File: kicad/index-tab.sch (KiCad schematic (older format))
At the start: 40 parts, among them J1 USB_C_Receptacle_USB2.0, SW1 SW_Push, U1 ATmega32U4-AU, Y1 16MHz

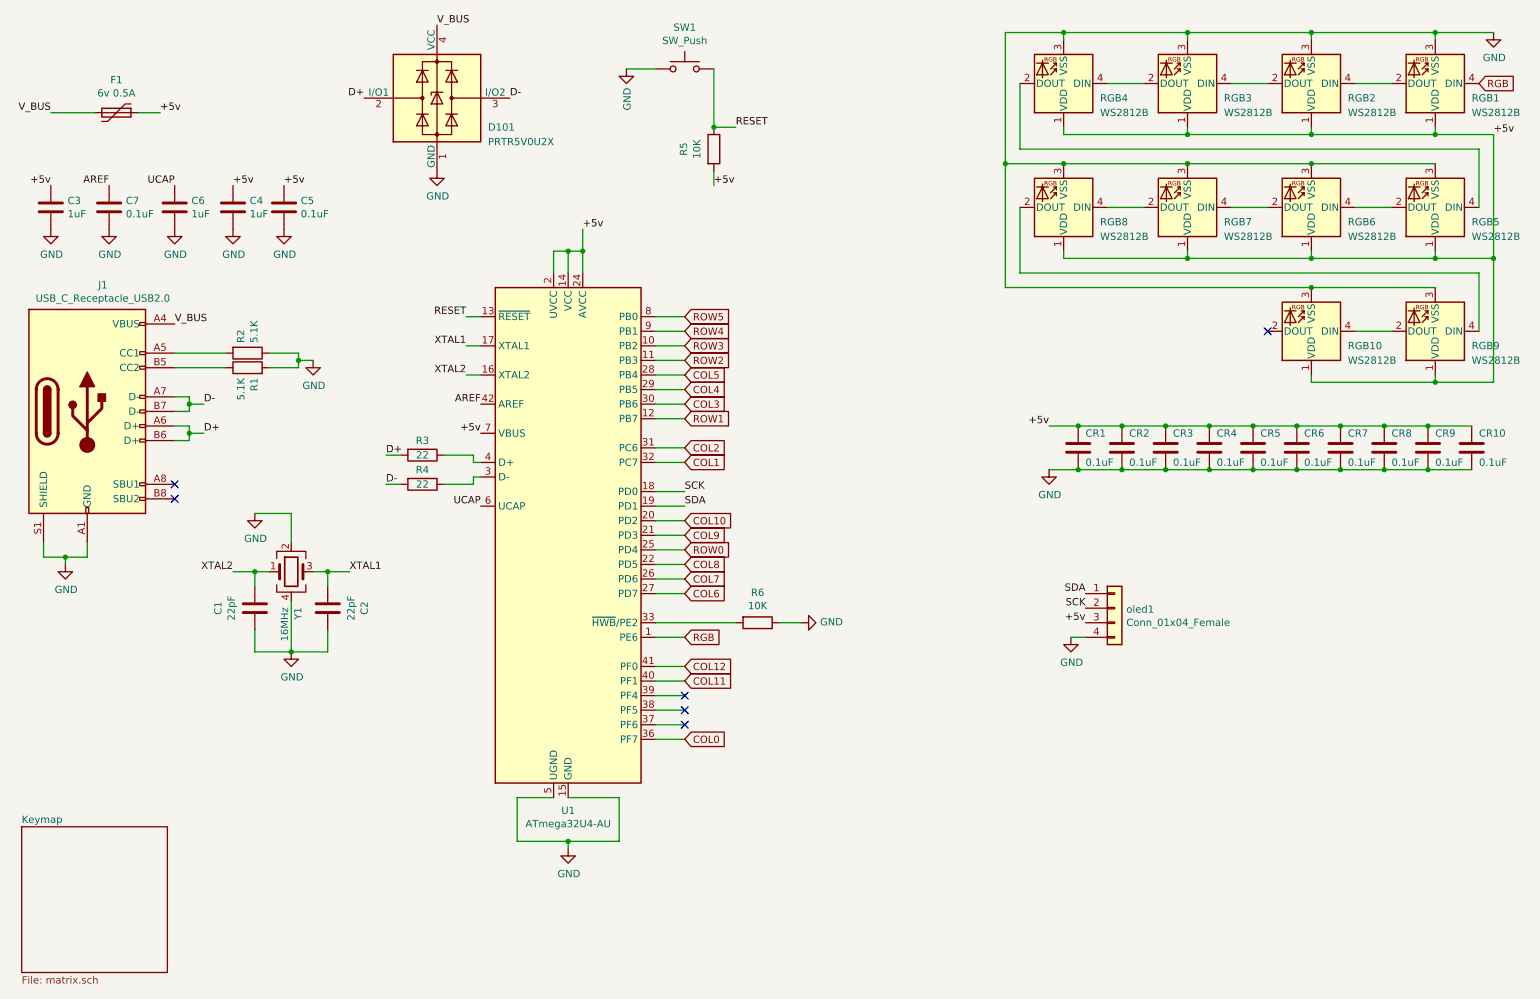
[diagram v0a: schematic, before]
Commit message: rev5: updated schematic
This is heavily inspired by Plain60 by evyd13
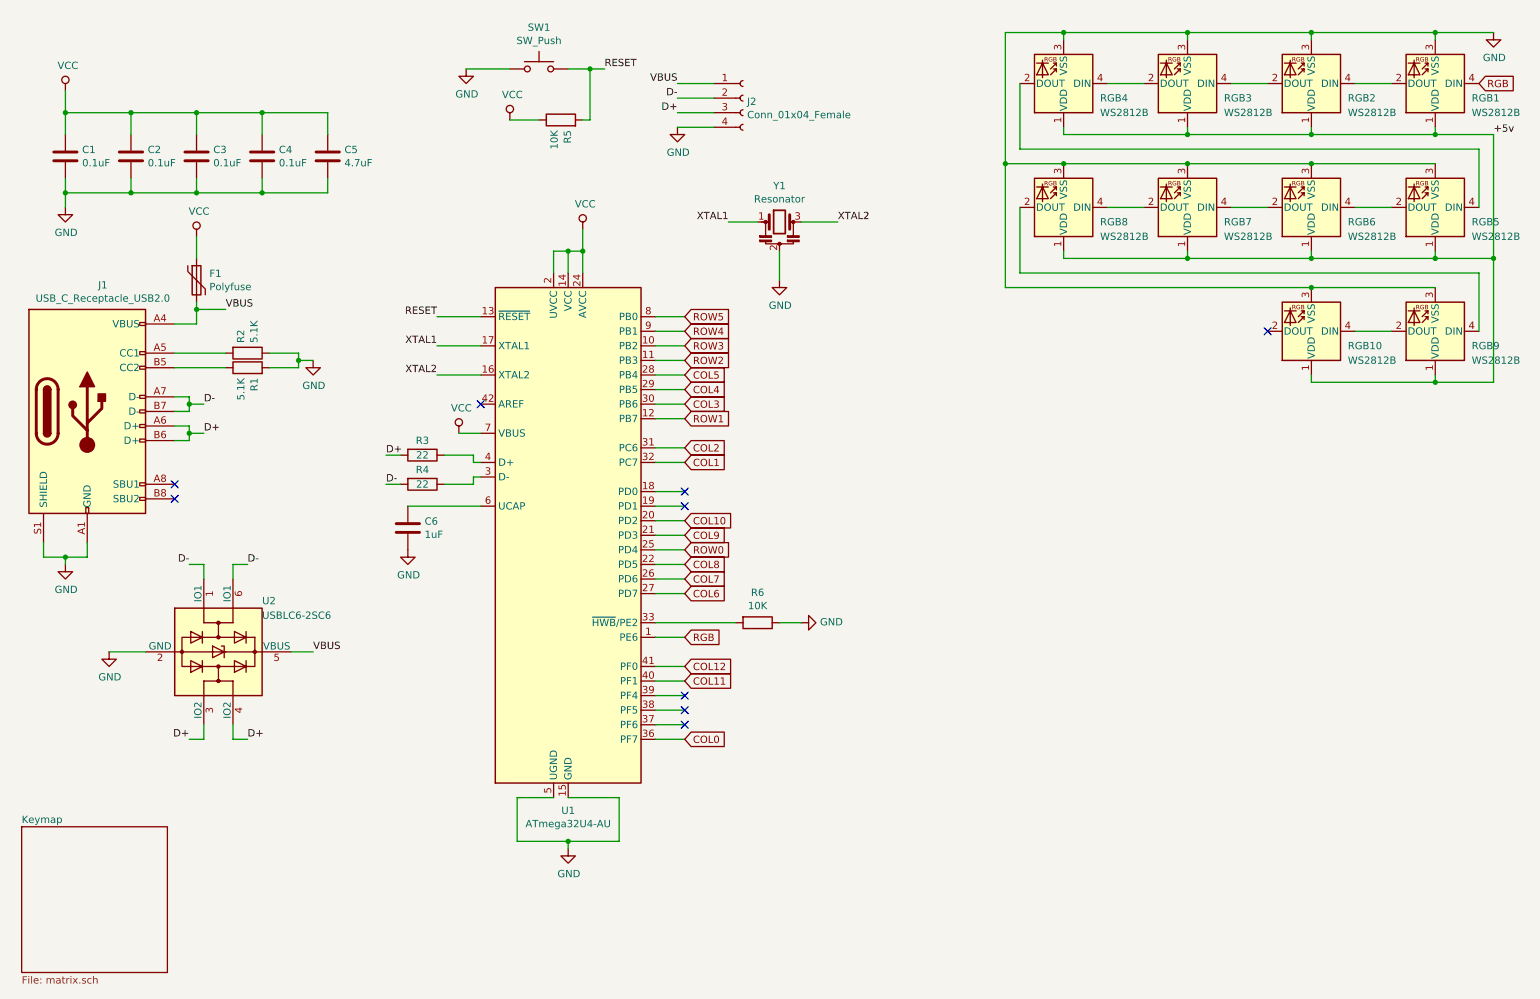
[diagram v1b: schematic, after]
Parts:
- removed C7, CR1, CR10, CR2, CR3, CR4, CR5, CR6, CR7, CR8, CR9: 0.1uF, Capacitor_SMD:C_0603_1608Metric_Pad1.05x0.95mm_HandSolder, symbol Device:C
- removed D101: PRTR5V0U2X, Package_TO_SOT_SMD:SOT-143, symbol Power_Protection:PRTR5V0U2X
- removed Y1: 16MHz, Crystal:Crystal_SMD_3225-4Pin_3.2x2.5mm_HandSoldering, symbol Device:Crystal_GND24
- removed oled1: Conn_01x04_Female, Connector_PinSocket_2.00mm:PinSocket_1x04_P2.00mm_Vertical, symbol Connector_Generic:Conn_01x04
- added J2: Conn_01x04_Female, index-tab:JST_SH_SM04B-SRSS-TB_1x04-1MP_P1.00mm_Horizontal, symbol Connector:Conn_01x04_Female
- added U2: USBLC6-2SC6, Package_TO_SOT_SMD:SOT-23-6, symbol Power_Protection:USBLC6-2SC6
- added Y1: Resonator, Crystal:Resonator_SMD_muRata_CSTxExxV-3Pin_3.0x1.1mm_HandSoldering, symbol Device:Resonator
- C1, C2: value 22pF -> 0.1uF; footprint Capacitor_SMD:C_0603_1608Metric_Pad1.05x0.95mm_HandSolder -> Capacitor_SMD:C_0603_1608Metric
- C3, C4: value 1uF -> 0.1uF; footprint Capacitor_SMD:C_0603_1608Metric_Pad1.05x0.95mm_HandSolder -> Capacitor_SMD:C_0603_1608Metric
- C5: value 0.1uF -> 4.7uF; footprint Capacitor_SMD:C_0603_1608Metric_Pad1.05x0.95mm_HandSolder -> Capacitor_SMD:C_0603_1608Metric
- C6: footprint Capacitor_SMD:C_0603_1608Metric_Pad1.05x0.95mm_HandSolder -> Capacitor_SMD:C_0603_1608Metric
- F1: value 6v 0.5A -> Polyfuse; footprint Fuse:Fuse_0805_2012Metric_Pad1.15x1.40mm_HandSolder -> Fuse:Fuse_0603_1608Metric
- R1, R2, R3, R4, R5, R6: footprint Resistor_SMD:R_0603_1608Metric_Pad1.05x0.95mm_HandSolder -> Resistor_SMD:R_0603_1608Metric
- SW1: footprint Button_Switch_SMD:SW_SPST_CK_RS282G05A3 -> Button_Switch_SMD:SW_DIP_SPSTx01_Slide_6.7x4.1mm_W6.73mm_P2.54mm_LowProfile_JPin
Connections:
- net +5v: no longer C3.1, C4.1, C5.1, F1.1, R5.2, U1.14 (VCC), U1.2 (UVCC), U1.24 (AVCC), U1.34 (VCC), U1.44 (AVCC), U1.7 (VBUS)
- net D+: now also J2.3 (Pin_3), U2.3 (IO2), U2.4 (IO2)
- net D-: now also J2.2 (Pin_2), U2.1 (IO1), U2.6 (IO1)
- net GND: now also C2.2, C6.1, J2.4 (Pin_4), U2.2 (GND), Y1.2; no longer C2.1, C6.2
- net RESET: now also R5.2; no longer R5.1
- net XTAL1: now also Y1.1; no longer C2.2
- net XTAL2: now also Y1.3; no longer C1.1
- net AREF: no longer names the net of U1.42 (AREF)
- net SCK: no longer names the net of U1.18 (PD0)
- net SDA: no longer names the net of U1.19 (PD1)
- net UCAP: no longer names the net of U1.6 (UCAP)
- net UCAP: now also C6.2; no longer C6.1
- net V_BUS renamed VBUS
- net VBUS: now also J2.1 (Pin_1), U2.5 (VBUS)
- new net VCC: C1.1, C2.1, C3.1, C4.1, C5.1, F1.1, R5.1, U1.14 (VCC), U1.2 (UVCC), U1.24 (AVCC), U1.34 (VCC), U1.44 (AVCC), U1.7 (VBUS)
- no-connect marks 6 -> 9

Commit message: rev5: MCU schematic and pcb should be done
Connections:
- net +5v is gone; now on net VCC: RGB1.1 (VDD), RGB10.1 (VDD), RGB2.1 (VDD), RGB3.1 (VDD), RGB4.1 (VDD), RGB5.1 (VDD), RGB6.1 (VDD), RGB7.1 (VDD), RGB8.1 (VDD), RGB9.1 (VDD)
- net COL8: now also U1.25 (PD4); no longer U1.22 (PD5)
- net COL9: now also U1.22 (PD5); no longer U1.21 (PD3)
- net D+: no longer J1.A6 (D+), J1.B6 (D+), J2.3 (Pin_3), U2.3 (IO2)
- net D-: no longer J1.A7 (D-), J1.B7 (D-), J2.2 (Pin_2), U2.1 (IO1)
- net ROW0: now also U1.21 (PD3); no longer U1.25 (PD4)
- new net USB_D+: J1.A6 (D+), J1.B6 (D+), J2.3 (Pin_3), U2.3 (IO2)
- new net USB_D-: J1.A7 (D-), J1.B7 (D-), J2.2 (Pin_2), U2.1 (IO1)
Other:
- moved on the sheet: R1, R2
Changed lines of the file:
@@
 Text GLabel 5300 3450 2    50   Input ~ 0
 ROW1
-Text GLabel 5300 4350 2    50   Input ~ 0
+Text GLabel 5300 4250 2    50   Input ~ 0
 ROW0
 $Comp
@@
 Text GLabel 5300 4150 2    50   Input ~ 0
 COL10
-Text GLabel 5300 4250 2    50   Input ~ 0
+Text GLabel 5300 4450 2    50   Input ~ 0
 COL9
-Text GLabel 5300 4450 2    50   Input ~ 0
+Text GLabel 5300 4350 2    50   Input ~ 0
 COL8
 Text GLabel 5300 4550 2    50   Input ~ 0
@@
 Text GLabel 10750 1150 2    50   Input ~ 0
 RGB
-Text Label 10850 1500 0    50   ~ 0
-+5v
 $Comp
 L power:GND #PWR0106
@@
 	1900 3350 2000 3350
 Text Label 2000 3350 0    50   ~ 0
-D-
+USB_D-
 Text Label 2000 3550 0    50   ~ 0
-D+
+USB_D+
 Wire Wire Line
 	1900 3500 1900 3550
@@
 Wire Wire Line
 	1900 3500 1800 3500
-Wire Wire Line
-	1800 3100 2150 3100
-Wire Wire Line
-	2150 3000 1800 3000
-Connection ~ 2650 3050
-Wire Wire Line
-	2650 3000 2650 3050
-Wire Wire Line
-	2450 3000 2650 3000
-Wire Wire Line
-	2650 3050 2750 3050
-Wire Wire Line
-	2650 3100 2650 3050
-Wire Wire Line
-	2450 3100 2650 3100
+Connection ~ 2850 3050
+Wire Wire Line
+	2850 3000 2850 3050
+Wire Wire Line
+	2650 3000 2850 3000
+Wire Wire Line
+	2850 3050 2950 3050
+Wire Wire Line
+	2850 3100 2850 3050
+Wire Wire Line
+	2650 3100 2850 3100
 $Comp
 L Device:R R2
 U 1 1 5E4988A3
-P 2300 3000
-F 0 "R2" H 2230 2954 50  0000 R CNN
-F 1 "5.1K" H 2230 3045 50  0000 R CNN
-F 2 "Resistor_SMD:R_0603_1608Metric" V 2230 3000 50  0001 C CNN
-F 3 "~" H 2300 3000 50  0001 C CNN
-	1    2300 3000
+P 2500 3000
+F 0 "R2" H 2430 2954 50  0000 R CNN
+F 1 "5.1K" H 2430 3045 50  0000 R CNN
+F 2 "Resistor_SMD:R_0603_1608Metric" V 2430 3000 50  0001 C CNN
+F 3 "~" H 2500 3000 50  0001 C CNN
+	1    2500 3000
 	0    1    1    0
 $EndComp
@@
 L Device:R R1
 U 1 1 5E496DB2
-P 2300 3100
-F 0 "R1" H 2230 3054 50  0000 R CNN
-F 1 "5.1K" H 2230 3145 50  0000 R CNN
-F 2 "Resistor_SMD:R_0603_1608Metric" V 2230 3100 50  0001 C CNN
-F 3 "~" H 2300 3100 50  0001 C CNN
-	1    2300 3100
+P 2500 3100
+F 0 "R1" H 2430 3054 50  0000 R CNN
+F 1 "5.1K" H 2430 3145 50  0000 R CNN
+F 2 "Resistor_SMD:R_0603_1608Metric" V 2430 3100 50  0001 C CNN
+F 3 "~" H 2500 3100 50  0001 C CNN
+	1    2500 3100
 	0    -1   -1   0
 $EndComp
@@
 L power:GND #PWR03
 U 1 1 5E49637F
-P 2750 3050
-F 0 "#PWR03" H 2750 2800 50  0001 C CNN
-F 1 "GND" H 2755 2877 50  0000 C CNN
-F 2 "" H 2750 3050 50  0001 C CNN
-F 3 "" H 2750 3050 50  0001 C CNN
-	1    2750 3050
+P 2950 3050
+F 0 "#PWR03" H 2950 2800 50  0001 C CNN
+F 1 "GND" H 2955 2877 50  0000 C CNN
+F 2 "" H 2950 3050 50  0001 C CNN
+F 3 "" H 2950 3050 50  0001 C CNN
+	1    2950 3050
 	1    0    0    -1
 $EndComp
@@
 	1600 5050 1350 5050
 Text Label 1900 4450 2    50   ~ 0
-D-
+USB_D-
 Text Label 2300 4450 0    50   ~ 0
 D-
@@
 D+
 Text Label 1900 5650 2    50   ~ 0
-D+
+USB_D+
 Wire Wire Line
 	1900 5650 2000 5650
@@
 $EndComp
 Text Label 5250 1350 2    50   ~ 0
-D+
+USB_D+
 Text Label 5250 1250 2    50   ~ 0
-D-
+USB_D-
 Text Label 5250 1150 2    50   ~ 0
 VBUS
@@
 Wire Wire Line
 	6100 2100 6350 2100
+$Comp
+L power:VCC #PWR0101
+U 1 1 60283534
+P 10850 1500
+F 0 "#PWR0101" H 10850 1350 50  0001 C CNN
+F 1 "VCC" H 10867 1673 50  0000 C CNN
+F 2 "" H 10850 1500 50  0001 C CNN
+F 3 "" H 10850 1500 50  0001 C CNN
+	1    10850 1500
+	1    0    0    -1
+$EndComp
+Connection ~ 10850 1500
+Wire Wire Line
+	1800 3000 2350 3000
+Wire Wire Line
+	1800 3100 2350 3100
 $EndSCHEMATC

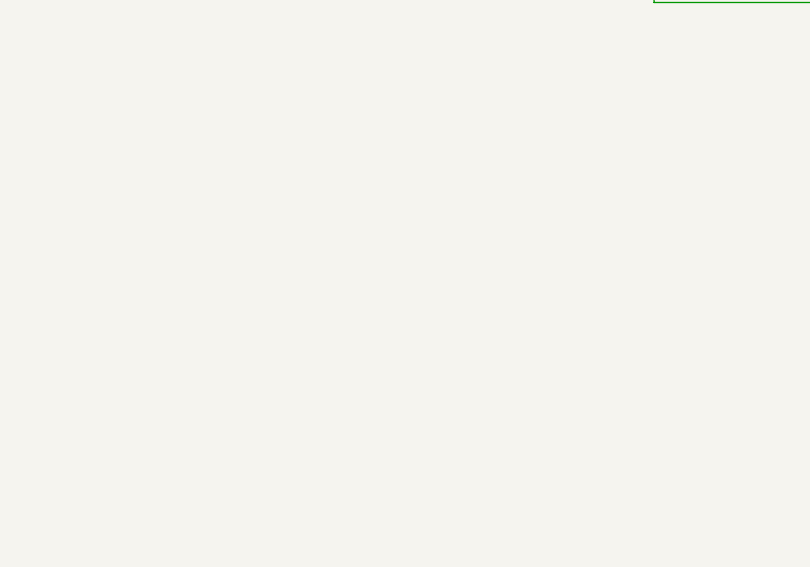
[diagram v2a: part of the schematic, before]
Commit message: rev5: fixed 2x2u and 7u stabs
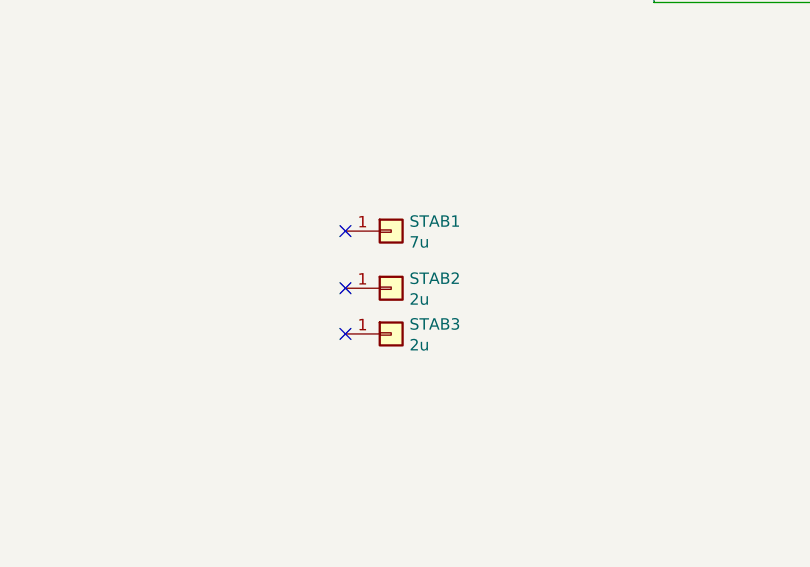
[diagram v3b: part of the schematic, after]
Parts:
- added STAB1: 7u, index-tab:MXOnly-7U-Hotswap, symbol Connector_Generic:Conn_01x01
- added STAB2, STAB3: 2u, index-tab:Stabilizer_MX_2u, symbol Connector_Generic:Conn_01x01
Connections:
- no-connect marks 9 -> 12
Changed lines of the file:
@@
 Sheet 1 2
 Title "Index Tab"
-Date "2020-02-06"
-Rev "4"
+Date "2021-02-13"
+Rev "5"
 Comp "Minimon"
 Comment1 ""
@@
 Wire Wire Line
 	1800 3100 2350 3100
+$Comp
+L Connector_Generic:Conn_01x01 STAB1
+U 1 1 6036E318
+P 8450 4200
+F 0 "STAB1" H 8530 4242 50  0000 L CNN
+F 1 "7u" H 8530 4151 50  0000 L CNN
+F 2 "index-tab:MXOnly-7U-Hotswap" H 8450 4200 50  0001 C CNN
+F 3 "~" H 8450 4200 50  0001 C CNN
+	1    8450 4200
+	1    0    0    -1
+$EndComp
+NoConn ~ 8250 4200
+NoConn ~ 8250 4450
+$Comp
+L Connector_Generic:Conn_01x01 STAB2
+U 1 1 60383A5A
+P 8450 4450
+F 0 "STAB2" H 8530 4492 50  0000 L CNN
+F 1 "2u" H 8530 4401 50  0000 L CNN
+F 2 "index-tab:Stabilizer_MX_2u" H 8450 4450 50  0001 C CNN
+F 3 "~" H 8450 4450 50  0001 C CNN
+	1    8450 4450
+	1    0    0    -1
+$EndComp
+$Comp
+L Connector_Generic:Conn_01x01 STAB3
+U 1 1 60383E39
+P 8450 4650
+F 0 "STAB3" H 8530 4692 50  0000 L CNN
+F 1 "2u" H 8530 4601 50  0000 L CNN
+F 2 "index-tab:Stabilizer_MX_2u" H 8450 4650 50  0001 C CNN
+F 3 "~" H 8450 4650 50  0001 C CNN
+	1    8450 4650
+	1    0    0    -1
+$EndComp
+NoConn ~ 8250 4650
 $EndSCHEMATC

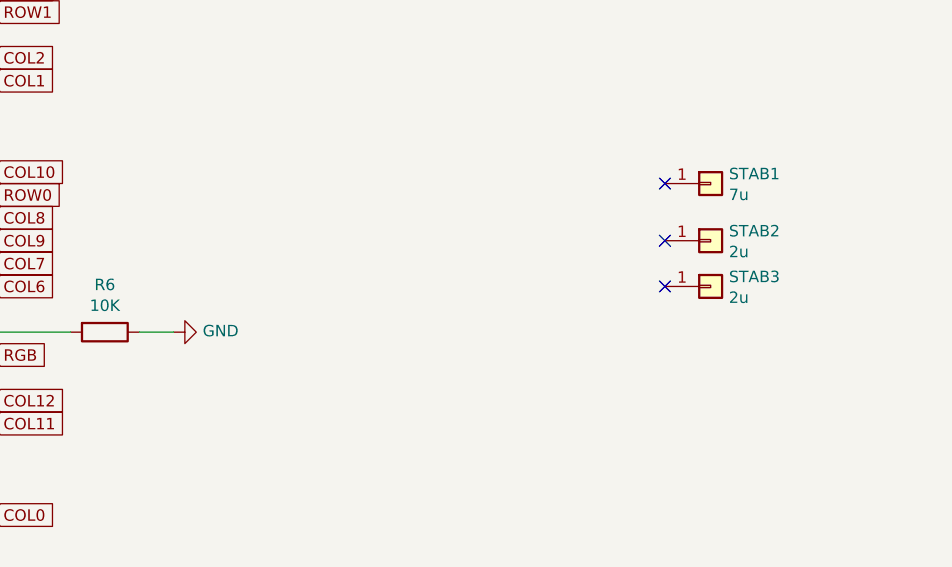
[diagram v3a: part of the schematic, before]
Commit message: rev5: fixed mounting holes
This time they are of the correct size for spacers!
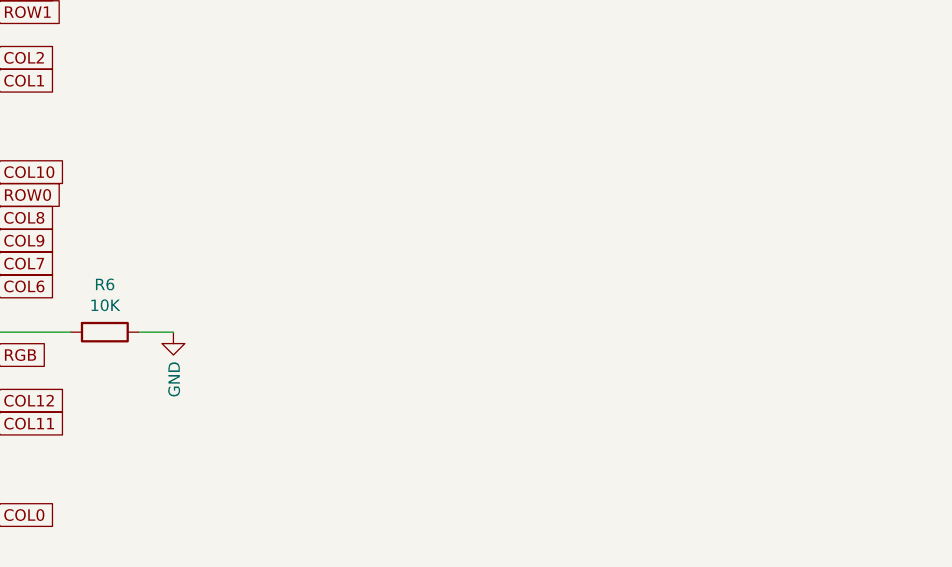
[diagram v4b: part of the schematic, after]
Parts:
- removed STAB1: 7u, index-tab:MXOnly-7U-Hotswap, symbol Connector_Generic:Conn_01x01
- removed STAB2, STAB3: 2u, index-tab:Stabilizer_MX_2u, symbol Connector_Generic:Conn_01x01
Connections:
- no-connect marks 12 -> 9
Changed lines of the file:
@@
 F 3 "" H 6100 4850 50  0001 C CNN
 	1    6100 4850
-	0    -1   -1   0
+	1    0    0    -1
 $EndComp
 Wire Wire Line
@@
 Wire Wire Line
 	1800 3100 2350 3100
-$Comp
-L Connector_Generic:Conn_01x01 STAB1
-U 1 1 6036E318
-P 8450 4200
-F 0 "STAB1" H 8530 4242 50  0000 L CNN
-F 1 "7u" H 8530 4151 50  0000 L CNN
-F 2 "index-tab:MXOnly-7U-Hotswap" H 8450 4200 50  0001 C CNN
-F 3 "~" H 8450 4200 50  0001 C CNN
-	1    8450 4200
-	1    0    0    -1
-$EndComp
-NoConn ~ 8250 4200
-NoConn ~ 8250 4450
-$Comp
-L Connector_Generic:Conn_01x01 STAB2
-U 1 1 60383A5A
-P 8450 4450
-F 0 "STAB2" H 8530 4492 50  0000 L CNN
-F 1 "2u" H 8530 4401 50  0000 L CNN
-F 2 "index-tab:Stabilizer_MX_2u" H 8450 4450 50  0001 C CNN
-F 3 "~" H 8450 4450 50  0001 C CNN
-	1    8450 4450
-	1    0    0    -1
-$EndComp
-$Comp
-L Connector_Generic:Conn_01x01 STAB3
-U 1 1 60383E39
-P 8450 4650
-F 0 "STAB3" H 8530 4692 50  0000 L CNN
-F 1 "2u" H 8530 4601 50  0000 L CNN
-F 2 "index-tab:Stabilizer_MX_2u" H 8450 4650 50  0001 C CNN
-F 3 "~" H 8450 4650 50  0001 C CNN
-	1    8450 4650
-	1    0    0    -1
-$EndComp
-NoConn ~ 8250 4650
 $EndSCHEMATC
